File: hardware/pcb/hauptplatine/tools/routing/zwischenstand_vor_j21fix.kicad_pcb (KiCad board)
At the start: 4 copper layers, 41 x 97 mm, 153 parts, among them J1 SJ-43504-SMT-TR, J20 FH12-30S-0.5SH(55), J21 503480-0600, J4 microSD, J6 USB, Q1 PMV48XPA2R, Q10 2N7002T, Q11 2N7002T, Q20 2N7002T, SW1 B3U-3000P, U10 MCP73871, U12 TUSB320LAI, U15 ESP32-S31-WROOM-1-N16R16V, U16 TPS22948, U17 CS43131-CNZR, U20 TPS61023DRL, U21 TPS2553DRV, U22 MAX17048G+T10, U3 D5V0L2B3T-7, U30 PCA9306DCUR, U31 SN74AXC1T45DRL, U32 SN74AXC1T45DRL, U33 SN74AXC1T45DRL, U34 TLV75518PDRV, U4 TLV75733PDRV, U5 PE1605C4A6, X1 22.5792MHz, X2 24.576MHz

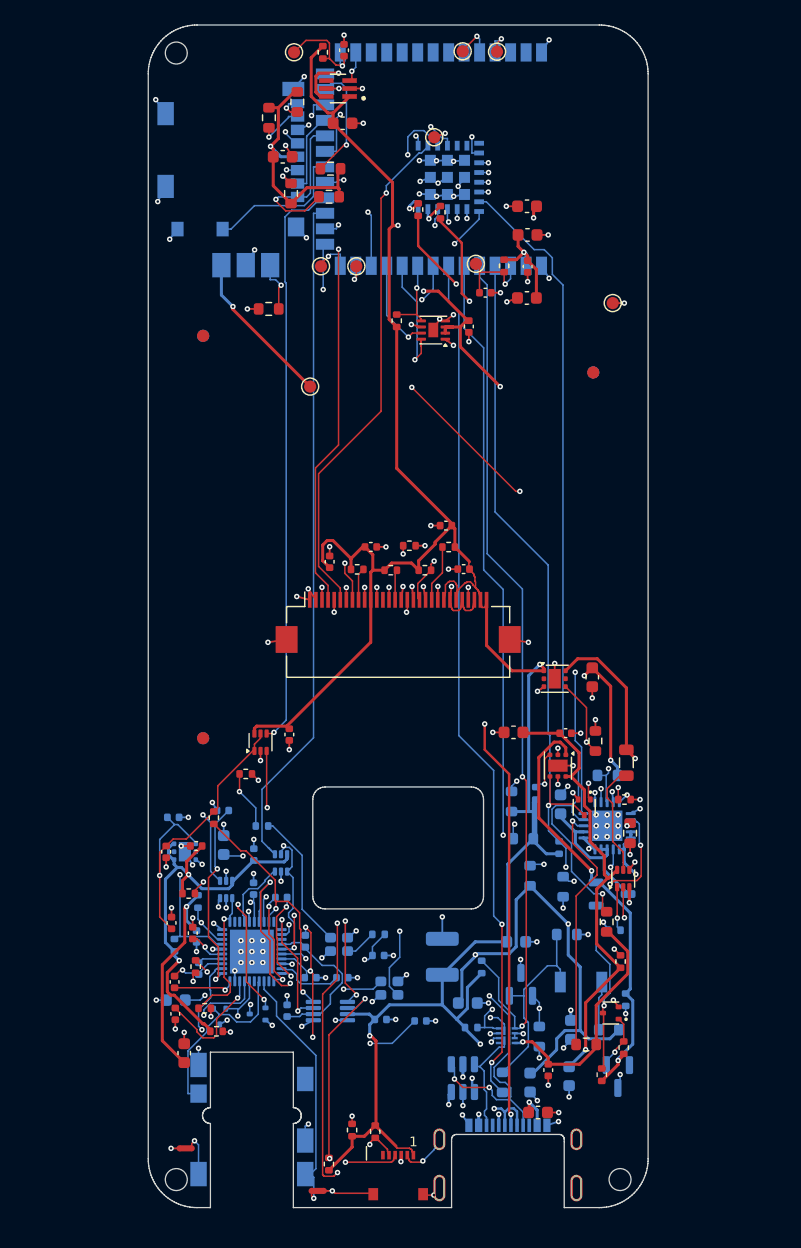
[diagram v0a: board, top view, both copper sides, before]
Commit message: Hauptplatine geroutet: Doku, Maße und Problemliste aktualisiert
Co-Authored-By: Claude Sonnet 5.5 <noreply@anthropic.com>
Claude-Session: https://claude.ai/code/session_01JifvE6gExGmwsJWDpfRrrS
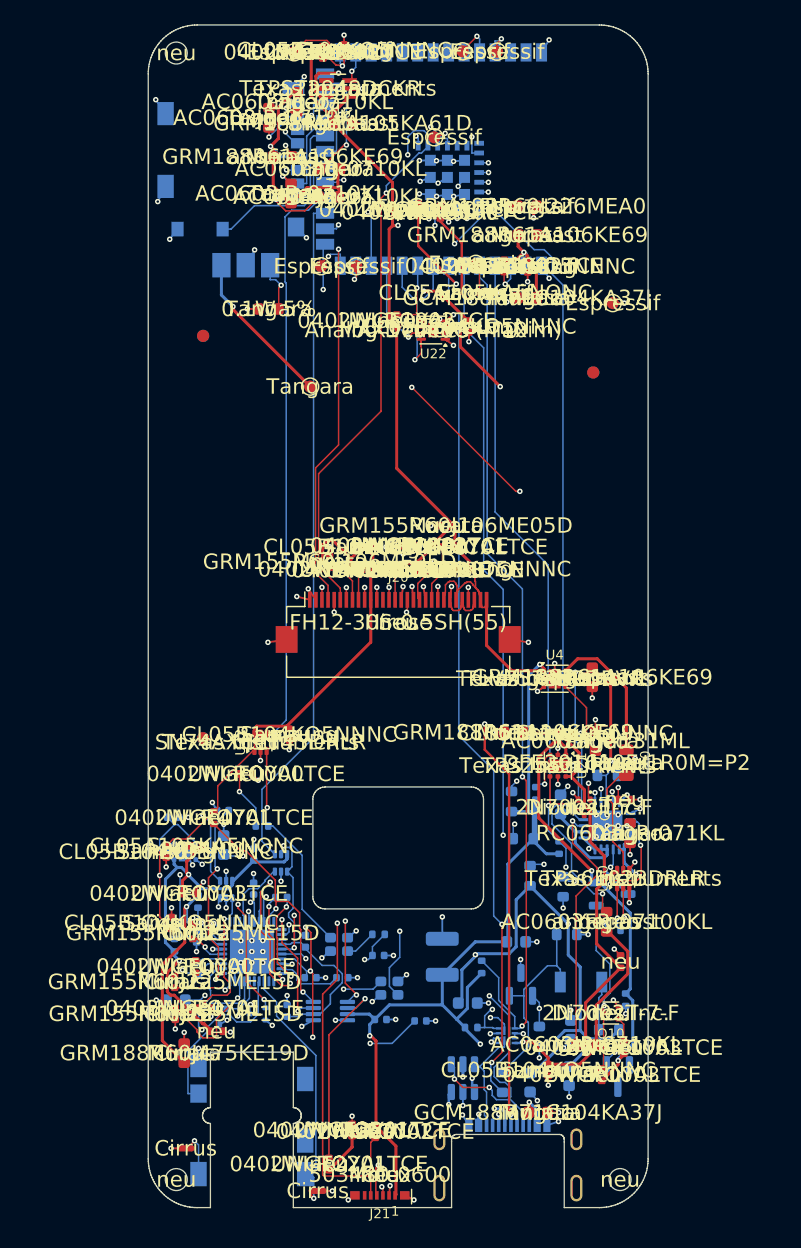
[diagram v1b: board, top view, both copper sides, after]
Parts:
- moved J21 1.55 mm to (98.5, 145.8), turned to 180 degrees
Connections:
- D10 pad 2: unconnected-(D10-NC_2-Pad2) -> (no net)
- J1 pad 6: unconnected-(J1-NC_6-Pad6) -> (no net)
- J20 pad 13: unconnected-(J20-NC_13-Pad13) -> (no net)
- J21 pad 6: unconnected-(J21-NC_6-Pad6) -> (no net)
- J6 pad A8: unconnected-(J6-NC_A8-PadA8) -> (no net)
- J6 pad B8: unconnected-(J6-NC_B8-PadB8) -> (no net)
- U12 pad 3: unconnected-(U12-NC_3-Pad3) -> (no net)
- U15 pad 26: unconnected-(U15-NC_26-Pad26) -> (no net)
- U15 pad 29: unconnected-(U15-NC_29-Pad29) -> (no net)
- U15 pad 30: unconnected-(U15-NC_30-Pad30) -> (no net)
- U15 pad 31: unconnected-(U15-NC_31-Pad31) -> (no net)
- U15 pad 32: unconnected-(U15-NC_32-Pad32) -> (no net)
- U15 pad 33: unconnected-(U15-NC_33-Pad33) -> (no net)
- U15 pad 34: unconnected-(U15-NC_34-Pad34) -> (no net)
- U15 pad 35: unconnected-(U15-NC_35-Pad35) -> (no net)
- U15 pad 38: unconnected-(U15-NC_38-Pad38) -> (no net)
- U15 pad 39: unconnected-(U15-NC_39-Pad39) -> (no net)
- U15 pad 42: unconnected-(U15-NC_42-Pad42) -> (no net)
- U15 pad 60: unconnected-(U15-NC_60-Pad60) -> (no net)
- U15 pad 61: unconnected-(U15-NC_61-Pad61) -> (no net)
- U16 pad 4: unconnected-(U16-NC_4-Pad4) -> (no net)
- U17 pad 12: unconnected-(U17-NC_12-Pad12) -> (no net)
- U17 pad 15: unconnected-(U17-NC_15-Pad15) -> (no net)
- U17 pad 29: unconnected-(U17-NC_29-Pad29) -> (no net)
- U17 pad 3: unconnected-(U17-NC_3-Pad3) -> (no net)
- U17 pad 32: unconnected-(U17-NC_32-Pad32) -> (no net)
- U17 pad 33: unconnected-(U17-NC_33-Pad33) -> (no net)
- U17 pad 40: unconnected-(U17-NC_40-Pad40) -> (no net)
- U34 pad 2: unconnected-(U34-NC_2-Pad2) -> (no net)
- U34 pad 5: unconnected-(U34-NC_5-Pad5) -> (no net)
- U4 pad 2: unconnected-(U4-NC_2-Pad2) -> (no net)
- U4 pad 5: unconnected-(U4-NC_5-Pad5) -> (no net)
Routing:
- net SCL: track 116.2 -> 125.7 mm, vias 6 -> 5
- net GND: track 128.7 -> 121.8 mm, vias 143 -> 144
- net SDA: track 106.2 -> 110.7 mm
- net CHG_STAT1: track 60.5 -> 57.6 mm
- net 3V3: track 308.0 -> 310.2 mm
- net WHEEL_INT: track 89.7 -> 90.9 mm, vias 4 -> 2
